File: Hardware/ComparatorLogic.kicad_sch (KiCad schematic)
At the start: 42 parts

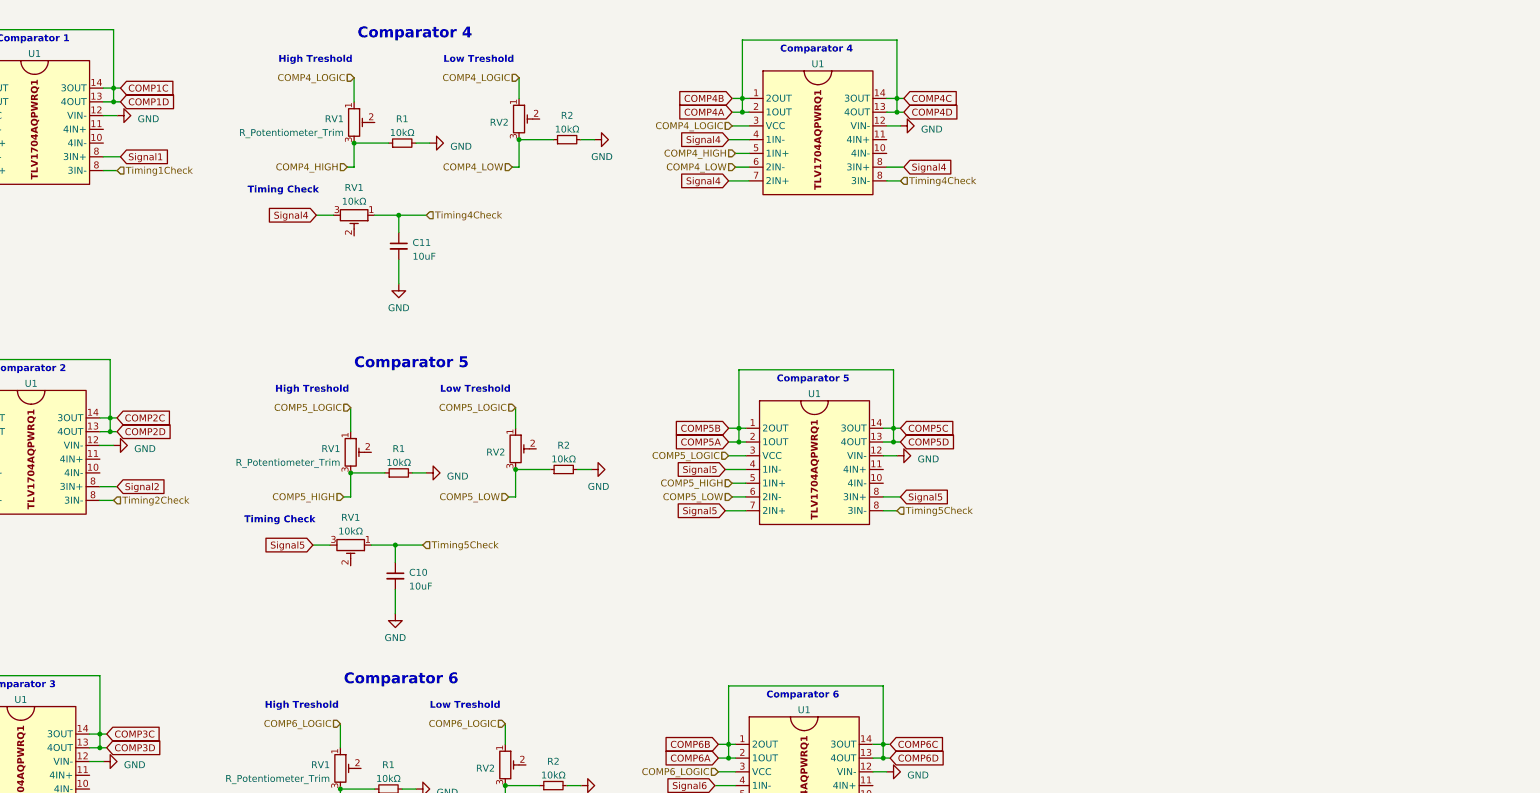
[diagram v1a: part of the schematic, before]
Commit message: Added changes to logic side for comparator inputs
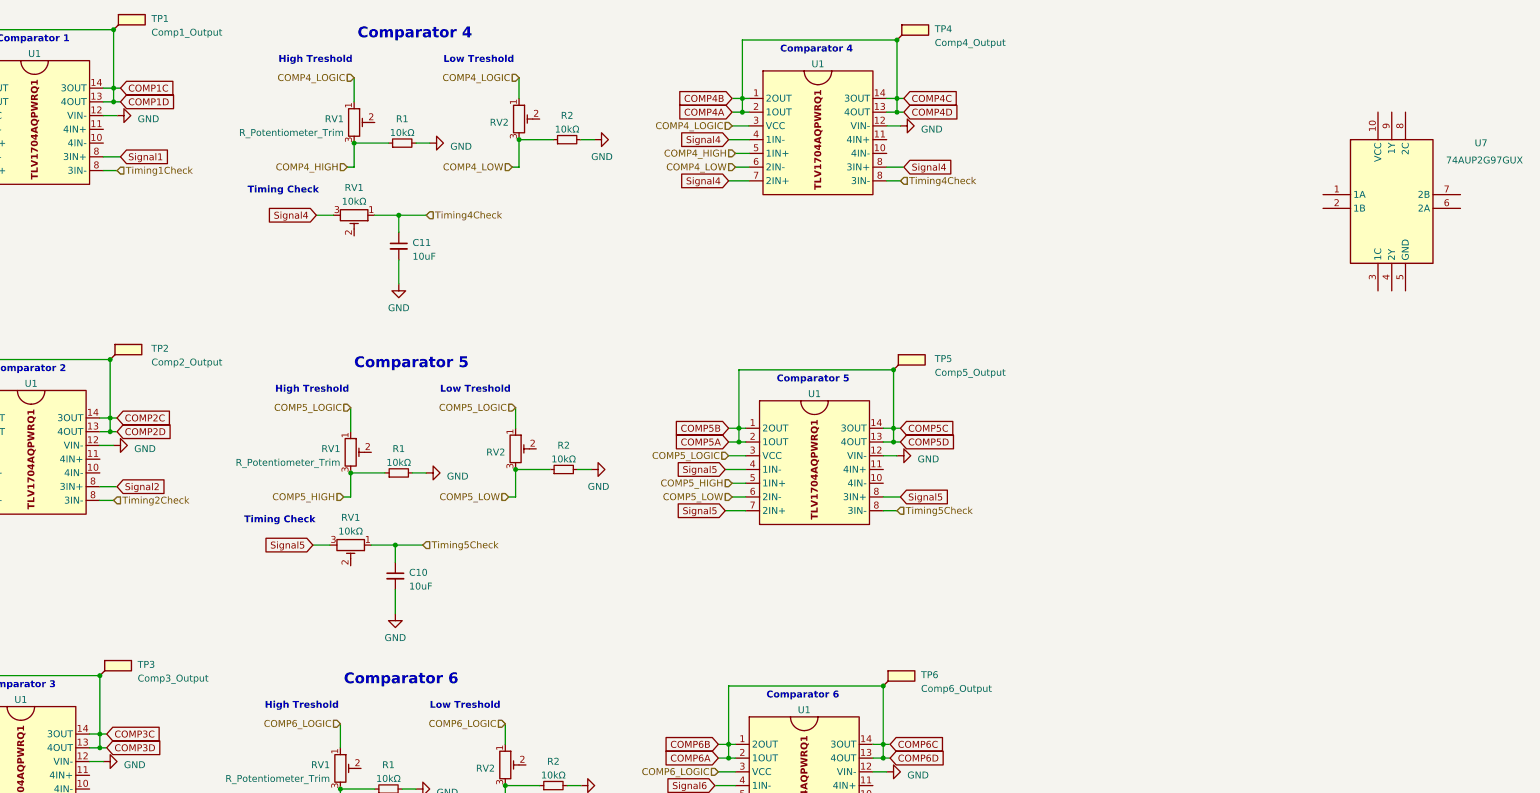
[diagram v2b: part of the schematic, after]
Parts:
- added TP1: Comp1_Output, TestPoint:TestPoint_Keystone_5015_Micro-Minature, symbol Connector:TestPoint_Flag
- added TP2: Comp2_Output, TestPoint:TestPoint_Keystone_5015_Micro-Minature, symbol Connector:TestPoint_Flag
- added TP3: Comp3_Output, TestPoint:TestPoint_Keystone_5015_Micro-Minature, symbol Connector:TestPoint_Flag
- added TP4: Comp4_Output, TestPoint:TestPoint_Keystone_5015_Micro-Minature, symbol Connector:TestPoint_Flag
- added TP5: Comp5_Output, TestPoint:TestPoint_Keystone_5015_Micro-Minature, symbol Connector:TestPoint_Flag
- added TP6: Comp6_Output, TestPoint:TestPoint_Keystone_5015_Micro-Minature, symbol Connector:TestPoint_Flag
- added U7: 74AUP2G97GUX, Package_DFN_QFN:QFN40P140X180X50-10N, symbol Logic_LevelTranslator:74AUP2G97GUX
- R1, R2: footprint (none) -> Resistor_SMD:R_0603_1608Metric
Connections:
- net COMP1A: now also TP1.1
- net COMP2A: now also TP2.1
- net COMP3A: now also TP3.1
- net COMP4A: now also TP4.1
- net COMP5A: now also TP5.1
- net COMP6A: now also TP6.1
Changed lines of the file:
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@@
   (junction (at 255.905 92.71) (diameter 0) (color 0 0 0 0)
   )
+  (junction (at 139.7 77.47) (diameter 0) (color 0 0 0 0)
+  )
   (junction (at 282.575 151.13) (diameter 0) (color 0 0 0 0)
   )
@@
   (junction (at 137.795 149.225) (diameter 0) (color 0 0 0 0)
   )
+  (junction (at 284.48 79.375) (diameter 0) (color 0 0 0 0)
+  )
   (junction (at 192.405 111.76) (diameter 0) (color 0 0 0 0)
   )
@@
   (junction (at 182.245 156.845) (diameter 0) (color 0 0 0 0)
   )
+  (junction (at 137.795 135.89) (diameter 0) (color 0 0 0 0)
+  )
   (junction (at 212.725 156.21) (diameter 0) (color 0 0 0 0)
   )
@@
   (junction (at 255.905 90.17) (diameter 0) (color 0 0 0 0)
   )
+  (junction (at 285.115 18.415) (diameter 0) (color 0 0 0 0)
+  )
   (junction (at 111.76 29.845) (diameter 0) (color 0 0 0 0)
   )
   (junction (at 190.5 170.18) (diameter 0) (color 0 0 0 0)
   )
+  (junction (at 282.575 137.795) (diameter 0) (color 0 0 0 0)
+  )
   (junction (at 37.465 154.94) (diameter 0) (color 0 0 0 0)
   )
@@
   (junction (at 48.26 48.895) (diameter 0) (color 0 0 0 0)
   )
+  (junction (at 140.335 16.51) (diameter 0) (color 0 0 0 0)
+  )
   (wire (pts (xy 254.635 100.33) (xy 257.175 100.33))
     (stroke (width 0) (type default))
@@
     )
   )
+  (symbol (lib_id "Connector:TestPoint_Flag") (at 139.7 77.47 0) (unit 1)
+    (in_bom yes) (on_board yes) (dnp no) (fields_autoplaced)
+    (property "Reference" "TP2" (at 147.32 75.438 0)
+      (effects (font (size 1.27 1.27)) (justify left))
+    )
+    (property "Value" "Comp2_Output" (at 147.32 77.978 0)
+      (effects (font (size 1.27 1.27)) (justify left))
+    )
+    (property "Footprint" "TestPoint:TestPoint_Keystone_5015_Micro-Minature" (at 144.78 77.47 0)
+      (effects (font (size 1.27 1.27)) hide)
+    )
+    (property "Datasheet" "~" (at 144.78 77.47 0)
+      (effects (font (size 1.27 1.27)) hide)
+    )
+    (pin "1")
+    (instances
+      (project "UTCB"
+        (path "/83d0f8a4-9dc2-453b-ad65-587c83c4dade/2d64236e-93fc-470c-b3e6-8835376edabc"
+          (reference "TP2") (unit 1)
+        )
+      )
+    )
+  )
   (symbol (lib_id "Device:R_Small") (at 48.895 35.56 90) (unit 1)
     (in_bom yes) (on_board yes) (dnp no)
@@
     )
   )
+  (symbol (lib_id "Connector:TestPoint_Flag") (at 284.48 79.375 0) (unit 1)
+    (in_bom yes) (on_board yes) (dnp no) (fields_autoplaced)
+    (property "Reference" "TP5" (at 292.1 77.343 0)
+      (effects (font (size 1.27 1.27)) (justify left))
+    )
+    (property "Value" "Comp5_Output" (at 292.1 79.883 0)
+      (effects (font (size 1.27 1.27)) (justify left))
+    )
+    (property "Footprint" "TestPoint:TestPoint_Keystone_5015_Micro-Minature" (at 289.56 79.375 0)
+      (effects (font (size 1.27 1.27)) hide)
+    )
+    (property "Datasheet" "~" (at 289.56 79.375 0)
+      (effects (font (size 1.27 1.27)) hide)
+    )
+    (pin "1")
+    (instances
+      (project "UTCB"
+        (path "/83d0f8a4-9dc2-453b-ad65-587c83c4dade/2d64236e-93fc-470c-b3e6-8835376edabc"
+          (reference "TP5") (unit 1)
+        )
+      )
+    )
+  )
   (symbol (lib_id "Device:C_Small") (at 193.04 56.515 0) (unit 1)
     (in_bom yes) (on_board yes) (dnp no) (fields_autoplaced)
@@
     )
   )
+  (symbol (lib_id "Connector:TestPoint_Flag") (at 285.115 18.415 0) (unit 1)
+    (in_bom yes) (on_board yes) (dnp no) (fields_autoplaced)
+    (property "Reference" "TP4" (at 292.1 16.383 0)
+      (effects (font (size 1.27 1.27)) (justify left))
+    )
+    (property "Value" "Comp4_Output" (at 292.1 18.923 0)
+      (effects (font (size 1.27 1.27)) (justify left))
+    )
+    (property "Footprint" "TestPoint:TestPoint_Keystone_5015_Micro-Minature" (at 290.195 18.415 0)
+      (effects (font (size 1.27 1.27)) hide)
+    )
+    (property "Datasheet" "~" (at 290.195 18.415 0)
+      (effects (font (size 1.27 1.27)) hide)
+    )
+    (pin "1")
+    (instances
+      (project "UTCB"
+        (path "/83d0f8a4-9dc2-453b-ad65-587c83c4dade/2d64236e-93fc-470c-b3e6-8835376edabc"
+          (reference "TP4") (unit 1)
+        )
+      )
+    )
+  )
+  (symbol (lib_id "Connector:TestPoint_Flag") (at 140.335 16.51 0) (unit 1)
+    (in_bom yes) (on_board yes) (dnp no) (fields_autoplaced)
+    (property "Reference" "TP1" (at 147.32 14.478 0)
+      (effects (font (size 1.27 1.27)) (justify left))
+    )
+    (property "Value" "Comp1_Output" (at 147.32 17.018 0)
+      (effects (font (size 1.27 1.27)) (justify left))
+    )
+    (property "Footprint" "TestPoint:TestPoint_Keystone_5015_Micro-Minature" (at 145.415 16.51 0)
+      (effects (font (size 1.27 1.27)) hide)
+    )
+    (property "Datasheet" "~" (at 145.415 16.51 0)
+      (effects (font (size 1.27 1.27)) hide)
+    )
+    (pin "1")
+    (instances
+      (project "UTCB"
+        (path "/83d0f8a4-9dc2-453b-ad65-587c83c4dade/2d64236e-93fc-470c-b3e6-8835376edabc"
+          (reference "TP1") (unit 1)
+        )
+      )
+    )
+  )
   (symbol (lib_id "Device:R_Small") (at 193.675 37.465 90) (unit 1)
     (in_bom yes) (on_board yes) (dnp no)
@@
     )
   )
+  (symbol (lib_id "Connector:TestPoint_Flag") (at 282.575 137.795 0) (unit 1)
+    (in_bom yes) (on_board yes) (dnp no) (fields_autoplaced)
+    (property "Reference" "TP6" (at 289.56 135.763 0)
+      (effects (font (size 1.27 1.27)) (justify left))
+    )
+    (property "Value" "Comp6_Output" (at 289.56 138.303 0)
+      (effects (font (size 1.27 1.27)) (justify left))
+    )
+    (property "Footprint" "TestPoint:TestPoint_Keystone_5015_Micro-Minature" (at 287.655 137.795 0)
+      (effects (font (size 1.27 1.27)) hide)
+    )
+    (property "Datasheet" "~" (at 287.655 137.795 0)
+      (effects (font (size 1.27 1.27)) hide)
+    )
+    (pin "1")
+    (instances
+      (project "UTCB"
+        (path "/83d0f8a4-9dc2-453b-ad65-587c83c4dade/2d64236e-93fc-470c-b3e6-8835376edabc"
+          (reference "TP6") (unit 1)
+        )
+      )
+    )
+  )
   (symbol (lib_id "power:GND") (at 192.405 124.46 0) (unit 1)
     (in_bom yes) (on_board yes) (dnp no) (fields_autoplaced)
@@
       (effects (font (size 1.27 1.27)))
     )
-    (property "Footprint" "" (at 48.26 96.52 0)
+    (property "Footprint" "Resistor_SMD:R_0603_1608Metric" (at 48.26 96.52 0)
       (effects (font (size 1.27 1.27)) hide)
     )
@@
     )
   )
+  (symbol (lib_id "Logic_LevelTranslator:74AUP2G97GUX") (at 363.855 46.99 0) (unit 1)
+    (in_bom yes) (on_board yes) (dnp no)
+    (property "Reference" "U7" (at 393.065 37.465 0)
+      (effects (font (size 1.27 1.27)))
+    )
+    (property "Value" "74AUP2G97GUX" (at 393.7 40.64 0)
+      (effects (font (size 1.27 1.27)))
+    )
+    (property "Footprint" "Package_DFN_QFN:QFN40P140X180X50-10N" (at 385.445 134.29 0)
+      (effects (font (size 1.27 1.27)) (justify left top) hide)
+    )
+    (property "Datasheet" "https://assets.nexperia.com/documents/data-sheet/74AUP2G97.pdf" (at 385.445 234.29 0)
+      (effects (font (size 1.27 1.27)) (justify left top) hide)
+    )
+    (property "Height" "0.5" (at 385.445 434.29 0)
+      (effects (font (size 1.27 1.27)) (justify left top) hide)
+    )
+    (property "Mouser Part Number" "771-74AUP2G97GUX" (at 385.445 534.29 0)
+      (effects (font (size 1.27 1.27)) (justify left top) hide)
+    )
+    (property "Mouser Price/Stock" "https://www.mouser.co.uk/ProductDetail/Nexperia/74AUP2G97GUX?qs=%252BRKXB2WKlSeRWu0tzkIbIQ%3D%3D" (at 385.445 634.29 0)
+      (effects (font (size 1.27 1.27)) (justify left top) hide)
+    )
+    (property "Manufacturer_Name" "Nexperia" (at 385.445 734.29 0)
+      (effects (font (size 1.27 1.27)) (justify left top) hide)
+    )
+    (property "Manufacturer_Part_Number" "74AUP2G97GUX" (at 385.445 834.29 0)
+      (effects (font (size 1.27 1.27)) (justify left top) hide)
+    )
+    (pin "1")
+    (pin "10")
+    (pin "2")
+    (pin "3")
+    (pin "4")
+    (pin "5")
+    (pin "6")
+    (pin "7")
+    (pin "8")
+    (pin "9")
+    (instances
+      (project "UTCB"
+        (path "/83d0f8a4-9dc2-453b-ad65-587c83c4dade/2d64236e-93fc-470c-b3e6-8835376edabc"
+          (reference "U7") (unit 1)
+        )
+      )
+    )
+  )
+  (symbol (lib_id "Connector:TestPoint_Flag") (at 137.795 135.89 0) (unit 1)
+    (in_bom yes) (on_board yes) (dnp no) (fields_autoplaced)
+    (property "Reference" "TP3" (at 144.78 133.858 0)
+      (effects (font (size 1.27 1.27)) (justify left))
+    )
+    (property "Value" "Comp3_Output" (at 144.78 136.398 0)
+      (effects (font (size 1.27 1.27)) (justify left))
+    )
+    (property "Footprint" "TestPoint:TestPoint_Keystone_5015_Micro-Minature" (at 142.875 135.89 0)
+      (effects (font (size 1.27 1.27)) hide)
+    )
+    (property "Datasheet" "~" (at 142.875 135.89 0)
+      (effects (font (size 1.27 1.27)) hide)
+    )
+    (pin "1")
+    (instances
+      (project "UTCB"
+        (path "/83d0f8a4-9dc2-453b-ad65-587c83c4dade/2d64236e-93fc-470c-b3e6-8835376edabc"
+          (reference "TP3") (unit 1)
+        )
+      )
+    )
+  )
   (symbol (lib_id "power:GND") (at 83.82 95.885 90) (unit 1)
     (in_bom yes) (on_board yes) (dnp no)
@@
       (effects (font (size 1.27 1.27)))
     )
-    (property "Footprint" "" (at 78.74 95.885 0)
+    (property "Footprint" "Resistor_SMD:R_0603_1608Metric" (at 78.74 95.885 0)
       (effects (font (size 1.27 1.27)) hide)
     )

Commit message: Removed a lot of unnecessary BJT logic, removed rotary switches for logic setting (set all to universal final 3.3v based logic)
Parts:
- removed U7: 74AUP2G97GUX, Package_DFN_QFN:QFN40P140X180X50-10N, symbol Logic_LevelTranslator:74AUP2G97GUX
- added R9: 1k, Resistor_SMD:R_0603_1608Metric, symbol Device:R_Small
- added TP22 (x2): COMP5_HIGH, TestPoint:TestPoint_Keystone_5015_Micro-Minature, symbol Connector:TestPoint_Flag
- added TP22: COMP4_TIMING, TestPoint:TestPoint_Keystone_5015_Micro-Minature, symbol Connector:TestPoint_Flag
- added TP22: COMP2_HIGH, TestPoint:TestPoint_Keystone_5015_Micro-Minature, symbol Connector:TestPoint_Flag
- added TP22 (x2): COMP4_HIGH, TestPoint:TestPoint_Keystone_5015_Micro-Minature, symbol Connector:TestPoint_Flag
- added TP22 (x2): COMP3_TIMING, TestPoint:TestPoint_Keystone_5015_Micro-Minature, symbol Connector:TestPoint_Flag
- added TP22: COMP2_TIMING, TestPoint:TestPoint_Keystone_5015_Micro-Minature, symbol Connector:TestPoint_Flag
- added TP22 (x2): COMP3_HIGH, TestPoint:TestPoint_Keystone_5015_Micro-Minature, symbol Connector:TestPoint_Flag
- added TP22: COMP6_TIMING, TestPoint:TestPoint_Keystone_5015_Micro-Minature, symbol Connector:TestPoint_Flag
- added TP22: COMP1_HIGH, TestPoint:TestPoint_Keystone_5015_Micro-Minature, symbol Connector:TestPoint_Flag
- added TP22: COMP1_TIMING, TestPoint:TestPoint_Keystone_5015_Micro-Minature, symbol Connector:TestPoint_Flag
- added TP22: COMP1_LOW, TestPoint:TestPoint_Keystone_5015_Micro-Minature, symbol Connector:TestPoint_Flag
- added TP22: COMP2_LOW, TestPoint:TestPoint_Keystone_5015_Micro-Minature, symbol Connector:TestPoint_Flag
- added TP22 (x2): COMP6_HIGH, TestPoint:TestPoint_Keystone_5015_Micro-Minature, symbol Connector:TestPoint_Flag
- added TP33: Failure_Check, TestPoint:TestPoint_Keystone_5015_Micro-Minature, symbol Connector:TestPoint_Flag
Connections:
- net COMP2A is gone; now on net COMP1A: TP2.1, U1.1 (2OUT), U1.13 (4OUT), U1.14 (3OUT), U1.2 (1OUT)
- net COMP3A is gone; now on net COMP1A: TP3.1, U1.1 (2OUT), U1.13 (4OUT), U1.14 (3OUT), U1.2 (1OUT)
- net COMP4A is gone; now on net COMP1A: TP4.1, U1.1 (2OUT), U1.13 (4OUT), U1.14 (3OUT), U1.2 (1OUT)
- net COMP5A is gone; now on net COMP1A: TP5.1, U1.1 (2OUT), U1.13 (4OUT), U1.14 (3OUT), U1.2 (1OUT)
- net COMP6A is gone; now on net COMP1A: TP6.1, U1.1 (2OUT), U1.13 (4OUT), U1.14 (3OUT), U1.2 (1OUT)
- net COMP1A: now also R9.2, TP33.1
- net COMP1_HIGH: now also TP22.1
- net COMP1_LOGIC: now also R9.1
- net COMP1_LOW: now also TP22.1
- net COMP2_HIGH: now also TP22.1
- net COMP2_LOW: now also TP22.1
- net COMP3_HIGH: now also TP22.1
- net COMP3_LOW: now also TP22.1
- net COMP4_HIGH: now also TP22.1
- net COMP4_LOW: now also TP22.1
- net COMP5_HIGH: now also TP22.1
- net COMP5_LOW: now also TP22.1
- net COMP6_HIGH: now also TP22.1
- net COMP6_LOW: now also TP22.1
- net Timing1Check: now also TP22.1
- net Timing2Check: now also TP22.1
- net Timing3Check: now also TP22.1
- net Timing4Check: now also TP22.1
- net Timing5Check: now also TP22.1
- net Timing6Check: now also TP22.1
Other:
- note added: "Failure Check"
- moved on the sheet: C10, C11, C6, C7, C8, C9, R1, R2, RV1, RV2, TP1, TP2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
